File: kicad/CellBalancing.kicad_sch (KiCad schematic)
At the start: 0 parts

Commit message: fixed cell layout, started making balancing circuitry
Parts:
- added C5: 1nF, symbol Device:C
- added C6: 10nF, symbol Device:C
- added C7: 22uF, symbol Device:C
- added C8, C9: 10uF, symbol Device:C
- added D1: LED, symbol Device:LED
- added L1: 2.2uH, symbol Device:L
- added R4: R, symbol Device:R
- added R5: 150, symbol Device:R
- added U15: ETA3000, Package_DFN_QFN:DFN-8-1EP_2x2mm_P0.5mm_EP0.9x1.3mm, symbol Battery_Management:ETA3000
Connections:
- new net: D1.1 (K), U15.6 (STAT)
- new net: D1.2 (A), R5.1
- new net: C5.1, R4.1, U15.7 (ISET)
- new net: C6.1, U15.5 (BIAS)
- new net: C6.2, L1.1, U15.3 (SW)
- new net: C7.1, R5.2, U15.2 (BATP)
- new net -Cell2: C8.1, C9.2, L1.2, U15.1 (BATC)
- new net Balance_1_2: U15.8 (EN)
- new net GND: C5.2, C7.2, C8.2, C9.1, R4.2, U15.4 (BATN), U15.9 (EP)

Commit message: .gitignore
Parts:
- added C10, C12, C17, C19, C23, C25, C28, C30, C33, C47, C50, C52, C55, C57, C60, C62, C65, C67: 10nF, symbol Device:C
- added C11, C18, C24, C29, C37, C51, C56, C61, C66: 22uF, symbol Device:C
- added C15, C16, C20, C22, C26, C27, C31, C32, C48, C49, C53, C54, C58, C59, C63, C64, C68, C69: 10uF, symbol Device:C
- added D10, D11, D12, D13, D14, D15, D16, D2, D3: LED, symbol Device:LED
- added L10, L11, L12, L2, L5, L6, L7, L8, L9: 2.2uH, symbol Device:L
- added R10, R12, R14, R16, R18, R20, R22, R6, R8: 160k, symbol Device:R
- added R11, R13, R15, R17, R19, R21, R23, R7, R9: 150, symbol Device:R
- added U16, U18, U19, U22, U23, U25, U26, U28, U29: ETA3000, Package_DFN_QFN:DFN-8-1EP_2x2mm_P0.5mm_EP0.9x1.3mm, symbol Battery_Management:ETA3000
- C5: value 1nF -> 10nF
- R4: value R -> 160k
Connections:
- net GND: now also C10.2, C17.2, C23.2, C28.2, C33.2, C50.2, C55.2, C60.2, C65.2, R10.2, R12.2, R14.2, R16.2, R18.2, R20.2, R22.2, R6.2, R8.2, U16.9 (EP), U18.9 (EP), U19.9 (EP), U22.9 (EP), U23.9 (EP), U25.9 (EP), U26.9 (EP), U28.9 (EP), U29.9 (EP); no longer C7.2, C8.2, C9.1, U15.4 (BATN)
- net -Cell2 renamed +Cell3
- net +Cell3: now also C11.2, C15.1, C16.2, C51.2, C53.1, C54.2, U16.4 (BATN), U25.4 (BATN)
- new net: D16.2 (A), R23.1
- new net: C66.1, R23.2, U29.2 (BATP)
- new net: C52.1, U25.5 (BIAS)
- new net: C52.2, L9.1, U25.3 (SW)
- new net: C51.1, R17.2, U25.2 (BATP)
- new net: D13.1 (K), U25.6 (STAT)
- new net: C50.1, R16.1, U25.7 (ISET)
- new net: D15.2 (A), R21.1
- new net: C61.1, R21.2, U28.2 (BATP)
- new net: D2.1 (K), U16.6 (STAT)
- new net: D2.2 (A), R7.1
- new net: D16.1 (K), U29.6 (STAT)
- new net: C18.1, R9.2, U18.2 (BATP)
- new net: C19.2, L5.1, U18.3 (SW)
- new net: C19.1, U18.5 (BIAS)
- new net: D3.1 (K), U18.6 (STAT)
- new net: C17.1, R8.1, U18.7 (ISET)
- new net: D15.1 (K), U28.6 (STAT)
- new net: C30.1, U22.5 (BIAS)
- new net: C30.2, L7.1, U22.3 (SW)
- new net: D12.1 (K), U23.6 (STAT)
- new net: D12.2 (A), R15.1
- new net: C65.1, R22.1, U29.7 (ISET)
- new net: C47.1, U23.5 (BIAS)
- new net: C47.2, L8.1, U23.3 (SW)
- new net: C56.1, R19.2, U26.2 (BATP)
- new net: C24.1, R11.2, U19.2 (BATP)
- new net: C60.1, R20.1, U28.7 (ISET)
- new net: C62.2, L11.1, U28.3 (SW)
- new net: C11.1, R7.2, U16.2 (BATP)
- new net: C12.2, L2.1, U16.3 (SW)
- new net: C12.1, U16.5 (BIAS)
- new net: C10.1, R6.1, U16.7 (ISET)
- new net: D14.1 (K), U26.6 (STAT)
- new net: D14.2 (A), R19.1
- new net: C57.2, L10.1, U26.3 (SW)
- new net: D13.2 (A), R17.1
- new net: C33.1, R14.1, U23.7 (ISET)
- new net: D11.1 (K), U22.6 (STAT)
- new net: D11.2 (A), R13.1
- new net: C37.1, R15.2, U23.2 (BATP)
- new net: C67.1, U29.5 (BIAS)
- new net: C67.2, L12.1, U29.3 (SW)
- new net: C29.1, R13.2, U22.2 (BATP)
- new net: C28.1, R12.1, U22.7 (ISET)
- new net: C57.1, U26.5 (BIAS)
- new net: C55.1, R18.1, U26.7 (ISET)
- new net: D3.2 (A), R9.1
- new net: C25.2, L6.1, U19.3 (SW)
- new net: C25.1, U19.5 (BIAS)
- new net: D10.1 (K), U19.6 (STAT)
- new net: C23.1, R10.1, U19.7 (ISET)
- new net: C62.1, U28.5 (BIAS)
- new net: D10.2 (A), R11.1
- new net +Cell2: C7.2, C8.2, C9.1, U15.4 (BATN)
- new net +Cell4: C15.2, C16.1, C18.2, C20.1, C22.2, C53.2, C54.1, C56.2, C58.1, C59.2, L2.2, L9.2, U16.1 (BATC), U18.4 (BATN), U25.1 (BATC), U26.4 (BATN)
- new net +Cell5: C20.2, C22.1, C24.2, C26.1, C27.2, C58.2, C59.1, C61.2, C63.1, C64.2, L10.2, L5.2, U18.1 (BATC), U19.4 (BATN), U26.1 (BATC), U28.4 (BATN)
- new net +Cell6: C26.2, C27.1, C29.2, C31.1, C32.2, C63.2, C64.1, C66.2, C68.1, C69.2, L11.2, L6.2, U19.1 (BATC), U22.4 (BATN), U28.1 (BATC), U29.4 (BATN)
- new net +Cell7: C31.2, C32.1, C37.2, C48.1, C49.2, C68.2, C69.1, L12.2, L7.2, U22.1 (BATC), U23.4 (BATN), U29.1 (BATC)
- new net -Cell7: C48.2, C49.1, L8.2, U23.1 (BATC)
- new net Balance_2_3: U16.8 (EN), U25.8 (EN)
- new net Balance_3_4: U18.8 (EN), U26.8 (EN)
- new net Balance_4_5: U19.8 (EN), U28.8 (EN)
- new net Balance_5_6: U22.8 (EN), U29.8 (EN)
- new net Balance_6_7: U23.8 (EN)
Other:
- moved on the sheet: C5, C6, C7, C8, C9, D1, L1, R4, R5, U15

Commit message: README
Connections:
- net +Cell3: no longer C51.2, C53.1, C54.2, U25.4 (BATN)
- net +Cell4: no longer C53.2, C54.1, C56.2, C58.1, C59.2, L9.2, U25.1 (BATC), U26.4 (BATN)
- net +Cell5: no longer C58.2, C59.1, C61.2, C63.1, C64.2, L10.2, U26.1 (BATC), U28.4 (BATN)
- net +Cell6: no longer C63.2, C64.1, L11.2, U28.1 (BATC)
- net Balance_2_3: no longer U25.8 (EN)
- net Balance_3_4: no longer U26.8 (EN)
- net Balance_4_5: no longer U28.8 (EN)
- net Balance_5_6: no longer U29.8 (EN)
- net -Cell7 renamed +Cell8
- net +Cell8: now also C51.2, C53.1, C54.2, U25.4 (BATN)
- new net +Cell10: C58.2, C59.1, C61.2, C63.1, C64.2, L10.2, U26.1 (BATC), U28.4 (BATN)
- new net +Cell9: C53.2, C54.1, C56.2, C58.1, C59.2, L9.2, U25.1 (BATC), U26.4 (BATN)
- new net -Cell10: C63.2, C64.1, L11.2, U28.1 (BATC)
- new net Balance_10_11: U29.8 (EN)
- new net Balance_7_8: U25.8 (EN)
- new net Balance_8_9: U26.8 (EN)
- new net Balance_9_10: U28.8 (EN)
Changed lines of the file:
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@@
     )
   )
-  (global_label "-Cell4" (shape input) (at 294.64 82.55 0) (fields_autoplaced)
+  (global_label "-Cell9" (shape input) (at 294.64 82.55 0) (fields_autoplaced)
     (effects (font (size 1.27 1.27)) (justify left))
     (property "Intersheetrefs" "${INTERSHEET_REFS}" (at 304.0961 82.55 0)
@@
     )
   )
-  (global_label "+Cell5" (shape input) (at 294.64 64.77 0) (fields_autoplaced)
-    (effects (font (size 1.27 1.27)) (justify left))
-    (property "Intersheetrefs" "${INTERSHEET_REFS}" (at 304.0961 64.77 0)
+  (global_label "+Cell10" (shape input) (at 294.64 64.77 0) (fields_autoplaced)
+    (effects (font (size 1.27 1.27)) (justify left))
+    (property "Intersheetrefs" "${INTERSHEET_REFS}" (at 305.3056 64.77 0)
       (effects (font (size 1.27 1.27)) (justify left) hide)
     )
@@
     )
   )
-  (global_label "Balance_5_6" (shape input) (at 323.85 72.39 180) (fields_autoplaced)
-    (effects (font (size 1.27 1.27)) (justify right))
-    (property "Intersheetrefs" "${INTERSHEET_REFS}" (at 308.9512 72.39 0)
+  (global_label "Balance_10_11" (shape input) (at 323.85 72.39 180) (fields_autoplaced)
+    (effects (font (size 1.27 1.27)) (justify right))
+    (property "Intersheetrefs" "${INTERSHEET_REFS}" (at 306.5322 72.39 0)
       (effects (font (size 1.27 1.27)) (justify right) hide)
     )
@@
     )
   )
-  (global_label "-Cell3" (shape input) (at 152.4 73.66 0) (fields_autoplaced)
+  (global_label "-Cell8" (shape input) (at 152.4 73.66 0) (fields_autoplaced)
     (effects (font (size 1.27 1.27)) (justify left))
     (property "Intersheetrefs" "${INTERSHEET_REFS}" (at 161.8561 73.66 0)
@@
     )
   )
-  (global_label "+Cell4" (shape input) (at 223.52 64.77 0) (fields_autoplaced)
+  (global_label "+Cell9" (shape input) (at 223.52 64.77 0) (fields_autoplaced)
     (effects (font (size 1.27 1.27)) (justify left))
     (property "Intersheetrefs" "${INTERSHEET_REFS}" (at 232.9761 64.77 0)
@@
     )
   )
-  (global_label "+Cell3" (shape input) (at 152.4 64.77 0) (fields_autoplaced)
+  (global_label "+Cell8" (shape input) (at 152.4 64.77 0) (fields_autoplaced)
     (effects (font (size 1.27 1.27)) (justify left))
     (property "Intersheetrefs" "${INTERSHEET_REFS}" (at 161.8561 64.77 0)
@@
     )
   )
-  (global_label "-Cell3" (shape input) (at 223.52 82.55 0) (fields_autoplaced)
+  (global_label "-Cell8" (shape input) (at 223.52 82.55 0) (fields_autoplaced)
     (effects (font (size 1.27 1.27)) (justify left))
     (property "Intersheetrefs" "${INTERSHEET_REFS}" (at 232.9761 82.55 0)
@@
     )
   )
-  (global_label "Balance_2_3" (shape input) (at 110.49 72.39 180) (fields_autoplaced)
+  (global_label "Balance_7_8" (shape input) (at 110.49 72.39 180) (fields_autoplaced)
     (effects (font (size 1.27 1.27)) (justify right))
     (property "Intersheetrefs" "${INTERSHEET_REFS}" (at 95.5912 72.39 0)
@@
     )
   )
-  (global_label "-Cell2" (shape input) (at 152.4 82.55 0) (fields_autoplaced)
+  (global_label "-Cell7" (shape input) (at 152.4 82.55 0) (fields_autoplaced)
     (effects (font (size 1.27 1.27)) (justify left))
     (property "Intersheetrefs" "${INTERSHEET_REFS}" (at 161.8561 82.55 0)
@@
     )
   )
-  (global_label "Balance_4_5" (shape input) (at 252.73 72.39 180) (fields_autoplaced)
-    (effects (font (size 1.27 1.27)) (justify right))
-    (property "Intersheetrefs" "${INTERSHEET_REFS}" (at 237.8312 72.39 0)
-      (effects (font (size 1.27 1.27)) (justify right) hide)
-    )
-  )
-  (global_label "-Cell5" (shape input) (at 294.64 73.66 0) (fields_autoplaced)
-    (effects (font (size 1.27 1.27)) (justify left))
-    (property "Intersheetrefs" "${INTERSHEET_REFS}" (at 304.0961 73.66 0)
+  (global_label "Balance_9_10" (shape input) (at 252.73 72.39 180) (fields_autoplaced)
+    (effects (font (size 1.27 1.27)) (justify right))
+    (property "Intersheetrefs" "${INTERSHEET_REFS}" (at 236.6217 72.39 0)
+      (effects (font (size 1.27 1.27)) (justify right) hide)
+    )
+  )
+  (global_label "-Cell10" (shape input) (at 294.64 73.66 0) (fields_autoplaced)
+    (effects (font (size 1.27 1.27)) (justify left))
+    (property "Intersheetrefs" "${INTERSHEET_REFS}" (at 305.3056 73.66 0)
       (effects (font (size 1.27 1.27)) (justify left) hide)
     )
@@
     )
   )
-  (global_label "-Cell4" (shape input) (at 223.52 73.66 0) (fields_autoplaced)
+  (global_label "-Cell9" (shape input) (at 223.52 73.66 0) (fields_autoplaced)
     (effects (font (size 1.27 1.27)) (justify left))
     (property "Intersheetrefs" "${INTERSHEET_REFS}" (at 232.9761 73.66 0)
@@
     )
   )
-  (global_label "Balance_3_4" (shape input) (at 181.61 72.39 180) (fields_autoplaced)
+  (global_label "Balance_8_9" (shape input) (at 181.61 72.39 180) (fields_autoplaced)
     (effects (font (size 1.27 1.27)) (justify right))
     (property "Intersheetrefs" "${INTERSHEET_REFS}" (at 166.7112 72.39 0)

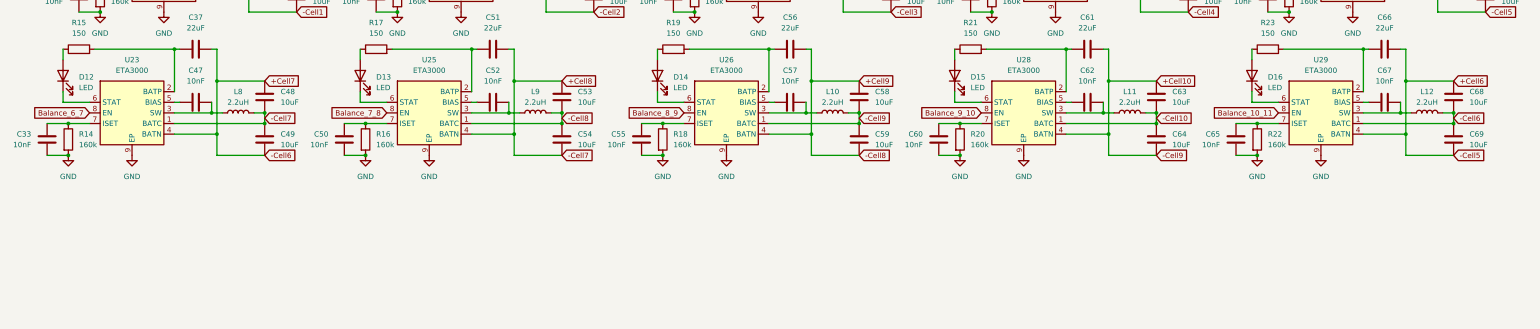
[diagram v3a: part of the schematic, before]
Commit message: implemented cell balancing up to 16S
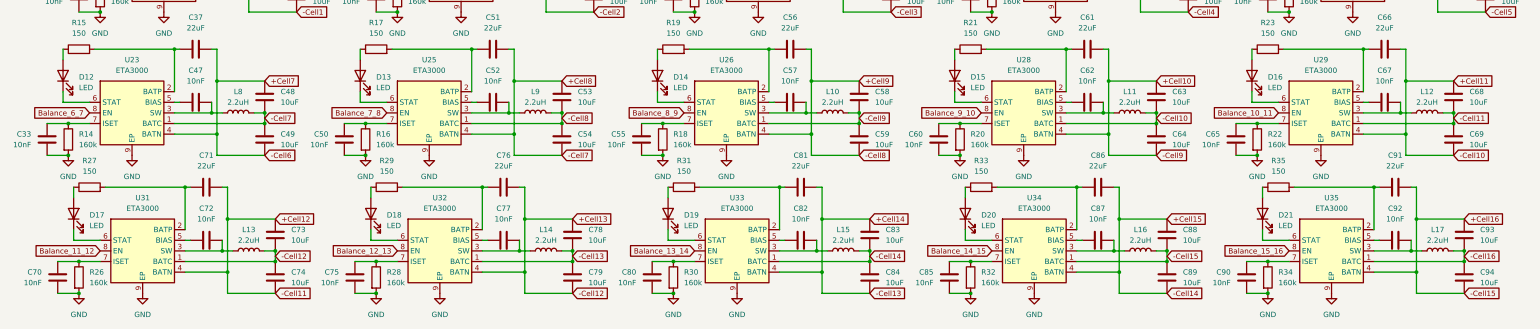
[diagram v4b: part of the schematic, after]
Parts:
- added C70, C72, C75, C77, C80, C82, C85, C87, C90, C92: 10nF, symbol Device:C
- added C71, C76, C81, C86, C91: 22uF, symbol Device:C
- added C73, C74, C78, C79, C83, C84, C88, C89, C93, C94: 10uF, symbol Device:C
- added D17, D18, D19, D20, D21: LED, symbol Device:LED
- added L13, L14, L15, L16, L17: 2.2uH, symbol Device:L
- added R26, R28, R30, R32, R34: 160k, symbol Device:R
- added R27, R29, R31, R33, R35: 150, symbol Device:R
- added U31, U32, U33, U34, U35: ETA3000, Package_DFN_QFN:DFN-8-1EP_2x2mm_P0.5mm_EP0.9x1.3mm, symbol Battery_Management:ETA3000
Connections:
- net +Cell6: no longer C66.2, C68.1, C69.2, U29.4 (BATN)
- net +Cell7: no longer C68.2, C69.1, L12.2, U29.1 (BATC)
- net GND: now also C70.2, C75.2, C80.2, C85.2, C90.2, R26.2, R28.2, R30.2, R32.2, R34.2, U31.9 (EP), U32.9 (EP), U33.9 (EP), U34.9 (EP), U35.9 (EP)
- net -Cell10 renamed +Cell11
- net +Cell11: now also C66.2, C68.1, C69.2, U29.4 (BATN)
- new net: C87.2, L16.1, U34.3 (SW)
- new net: C81.1, R31.2, U33.2 (BATP)
- new net: D17.2 (A), R27.1
- new net: C71.1, R27.2, U31.2 (BATP)
- new net: C82.2, L15.1, U33.3 (SW)
- new net: C82.1, U33.5 (BIAS)
- new net: D19.1 (K), U33.6 (STAT)
- new net: C80.1, R30.1, U33.7 (ISET)
- new net: C70.1, R26.1, U31.7 (ISET)
- new net: D17.1 (K), U31.6 (STAT)
- new net: C72.2, L13.1, U31.3 (SW)
- new net: C72.1, U31.5 (BIAS)
- new net: C87.1, U34.5 (BIAS)
- new net: C76.1, R29.2, U32.2 (BATP)
- new net: C75.1, R28.1, U32.7 (ISET)
- new net: C86.1, R33.2, U34.2 (BATP)
- new net: D20.1 (K), U34.6 (STAT)
- new net: C85.1, R32.1, U34.7 (ISET)
- new net: C91.1, R35.2, U35.2 (BATP)
- new net: D18.2 (A), R29.1
- new net: C92.2, L17.1, U35.3 (SW)
- new net: C92.1, U35.5 (BIAS)
- new net: D21.1 (K), U35.6 (STAT)
- new net: C90.1, R34.1, U35.7 (ISET)
- new net: D18.1 (K), U32.6 (STAT)
- new net: D20.2 (A), R33.1
- new net: D19.2 (A), R31.1
- new net: C77.2, L14.1, U32.3 (SW)
- new net: D21.2 (A), R35.1
- new net: C77.1, U32.5 (BIAS)
- new net +Cell12: C68.2, C69.1, C71.2, C73.1, C74.2, L12.2, U29.1 (BATC), U31.4 (BATN)
- new net +Cell13: C73.2, C74.1, C76.2, C78.1, C79.2, L13.2, U31.1 (BATC), U32.4 (BATN)
- new net +Cell14: C78.2, C79.1, C81.2, C83.1, C84.2, L14.2, U32.1 (BATC), U33.4 (BATN)
- new net +Cell15: C83.2, C84.1, C86.2, C88.1, C89.2, L15.2, U33.1 (BATC), U34.4 (BATN)
- new net +Cell16: C88.2, C89.1, C91.2, C93.1, C94.2, L16.2, U34.1 (BATC), U35.4 (BATN)
- new net -Cell16: C93.2, C94.1, L17.2, U35.1 (BATC)
- new net Balance_11_12: U31.8 (EN)
- new net Balance_12_13: U32.8 (EN)
- new net Balance_13_14: U33.8 (EN)
- new net Balance_14_15: U34.8 (EN)
- new net Balance_15_16: U35.8 (EN)
